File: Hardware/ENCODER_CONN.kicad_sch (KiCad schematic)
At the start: 22 parts, among them J11 PHB2.0-02-20PWZ, Q15 SI2305, Q17 SS8050, U31 MS2575T, U32 TXB0104RUTR, U33 MS2575T

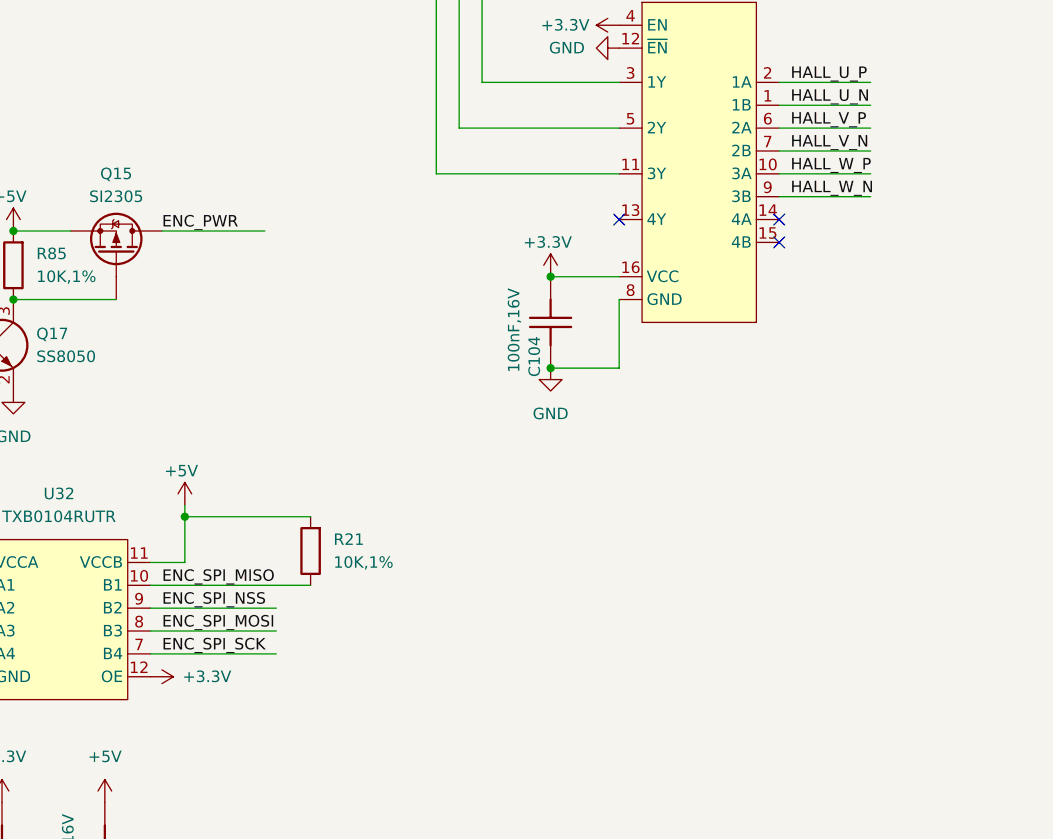
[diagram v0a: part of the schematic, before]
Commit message: 新增ESC IO引出，ESC CTR LED，EUI接口
编码器接口电源输出加保险，SPI加ESD
PY32ADC外部接口加ESD
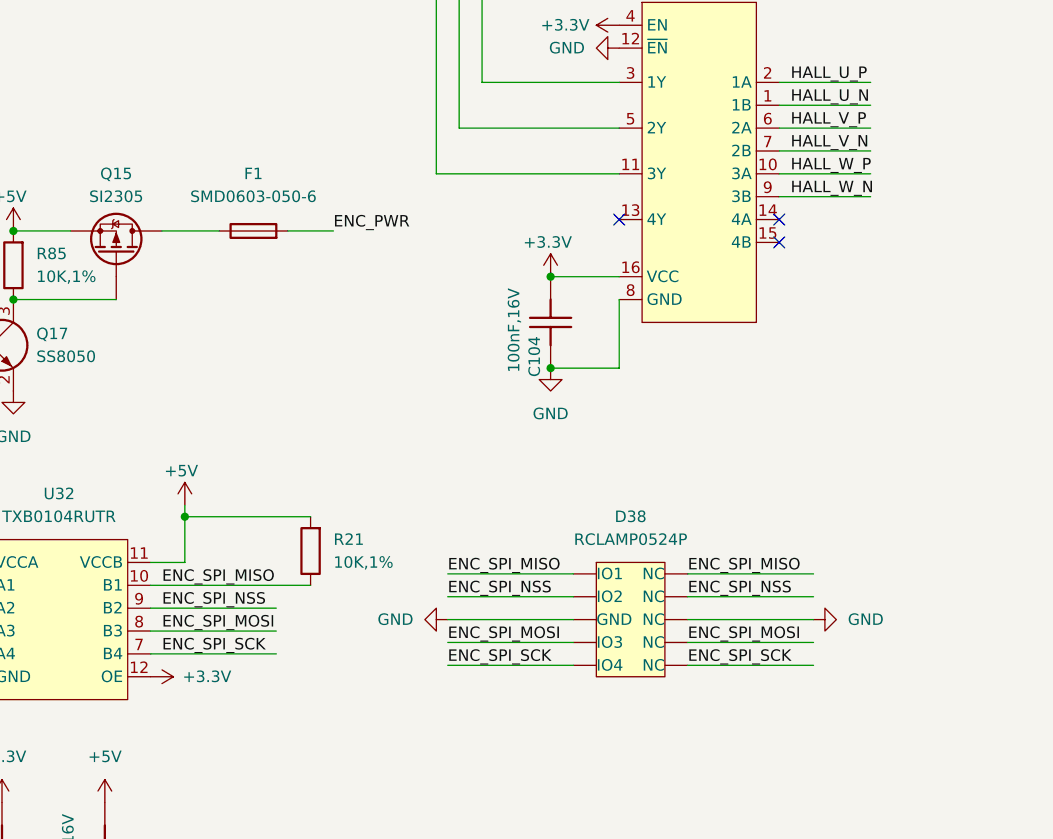
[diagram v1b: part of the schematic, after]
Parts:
- added D38: RCLAMP0524P, Package_DFN_QFN:Diodes_UDFN-10_1.0x2.5mm_P0.5mm, symbol HPM6280Foc:RCLAMP0524P
- added F1: SMD0603-050-6, Fuse:Fuse_0603_1608Metric, symbol HPM6280Foc:SMD0603-050-6
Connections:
- net ENC_PWR: now also F1.2; no longer Q15.3 (D)
- net ENC_SPI_MISO: now also D38.1 (IO1), D38.10 (NC)
- net ENC_SPI_MOSI: now also D38.4 (IO3), D38.7 (NC)
- net ENC_SPI_NSS: now also D38.2 (IO2), D38.9 (NC)
- net ENC_SPI_SCK: now also D38.5 (IO4), D38.6 (NC)
- net GND: now also D38.3 (GND), D38.8 (NC)
- new net: F1.1, Q15.3 (D)

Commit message: 拉线
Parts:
- renumbered C100 to C107, C103 to C110, C104 to C111, C105 to C112, C106 to C113, D38 to D39, F1 to F2, J11 to J12, NT21 to NT22, Q15 to Q16, Q17 to Q18, R21 to R22, R77 to R86, R78 to R87, R79 to R88, R80 to R89, R81 to R90, R82 to R91, R83 to R92, R84 to R93, R85 to R94, U31 to U35, U32 to U36, U33 to U37

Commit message: 修存档拉线
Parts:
- renumbered C107 to C79, C110 to C80, C111 to C81, C112 to C82, C113 to C83, J12 to J13, NT22 to NT21, Q16 to Q17, R86 to R79, R87 to R80, R88 to R81, R89 to R82, R90 to R83, R91 to R84, R92 to R85, R94 to R86, R93 to R87, R22 to R88, U35 to U39, U37 to U40, U36 to U41

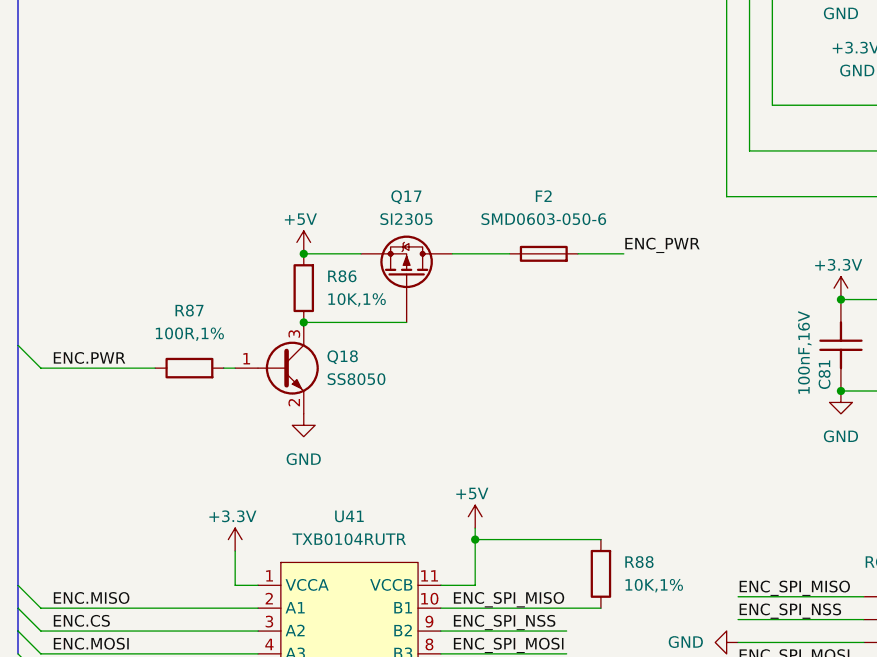
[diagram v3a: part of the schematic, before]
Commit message: 拉线，增加刹车电阻
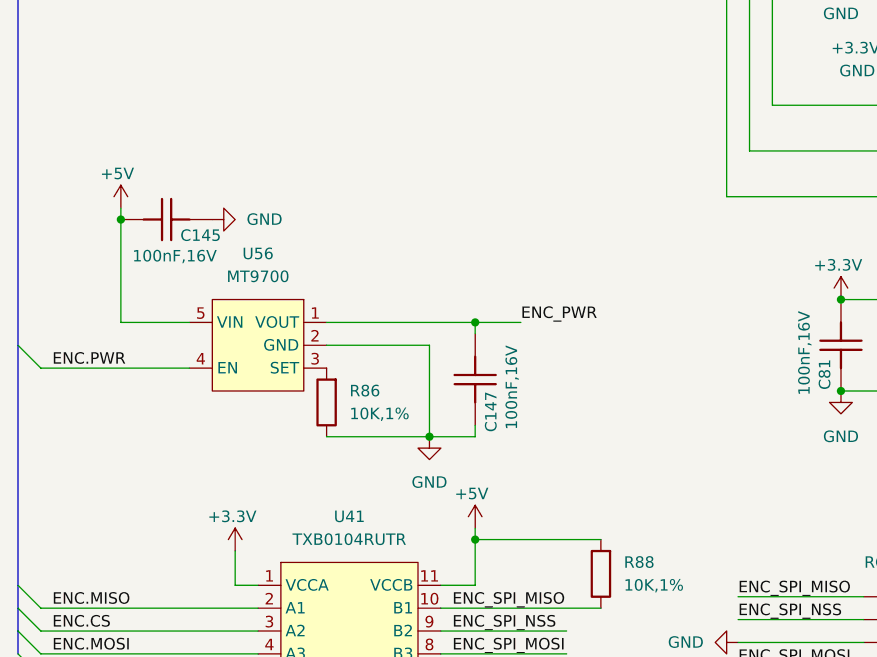
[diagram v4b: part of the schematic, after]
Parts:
- removed F2: SMD0603-050-6, Fuse:Fuse_0603_1608Metric, symbol HPM6280Foc:SMD0603-050-6
- removed Q17: SI2305, Package_TO_SOT_SMD:SOT-23-3, symbol HPM6280Foc:SI2305
- removed Q18: SS8050, Package_TO_SOT_SMD:SOT-23, symbol Transistor_BJT:SS8050
- removed R87: 100R,1%, Resistor_SMD:R_0402_1005Metric, symbol HPM6280Foc:0402WGF1000TCE
- added C145, C147: 100nF,16V, Capacitor_SMD:C_0402_1005Metric, symbol HPM6280Foc:CC0402KRX7R7BB104
- added U56: MT9700, Package_TO_SOT_SMD:SOT-23-5, symbol HPM6280Foc:MT9700
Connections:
- net +5V: now also C145.1, U56.5 (VIN); no longer R86.2
- net ENC.PWR: now also U56.4 (EN)
- net ENC_PWR: now also C147.2, U56.1 (VOUT)
- net GND: now also R86.1, C145.2, C147.1, U56.2 (GND)
- new net: R86.2, U56.3 (SET)

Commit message: PCB和foc_demo
PCB：
部分信号增加测试点
半桥增加栅极电容和RC吸收（待定），泄放mos是否需要栅极电容待测
软件：
增加foc_demo半成品
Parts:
- added TP1, TP10, TP12, TP14, TP16, TP18, TP3, TP4, TP6, TP8: ~, Library:test_point_0.5mm, symbol HPM6280Foc:test_point
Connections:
- net ENC.A: now also TP14.1
- net ENC.B: now also TP16.1
- net ENC.CLK: now also TP3.1
- net ENC.CS: now also TP4.1
- net ENC.MISO: now also TP6.1
- net ENC.MOSI: now also TP1.1
- net ENC.U: now also TP8.1
- net ENC.V: now also TP10.1
- net ENC.W: now also TP12.1
- net ENC.Z: now also TP18.1

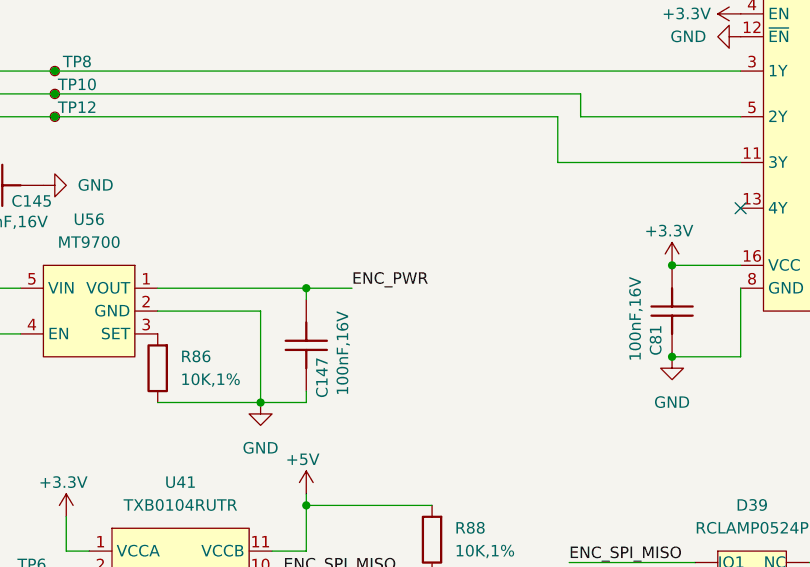
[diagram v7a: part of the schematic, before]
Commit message: PCB：风扇增加控制IO，泄放驱动增加使能引脚，485编码器电源接入控制
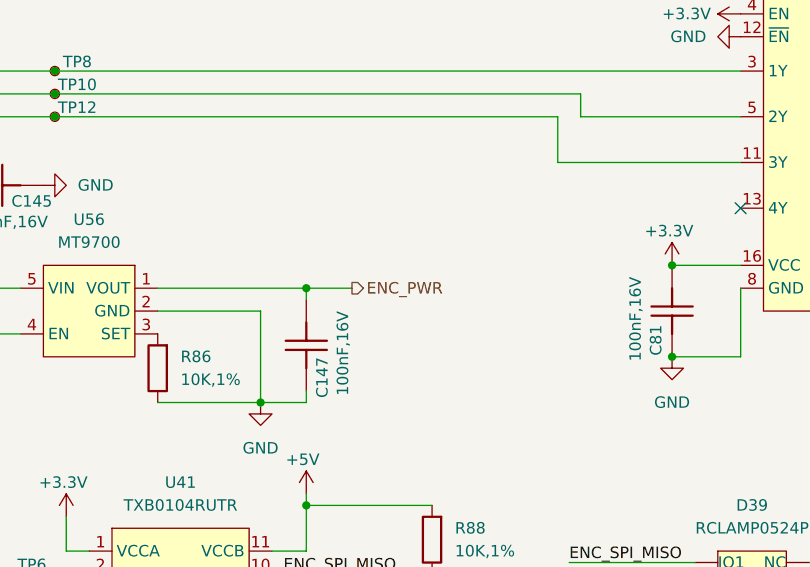
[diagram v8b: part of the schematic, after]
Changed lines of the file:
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@@
-		)
-	)
-	(label "ENC_PWR"
-		(at 85.09 107.95 0)
-		(effects
-			(font
-				(size 1.27 1.27)
-			)
-			(justify left bottom)
 		)
 	)
@@
 		)
 	)
+	(hierarchical_label "ENC_PWR"
+		(shape output)
+		(at 85.09 107.95 0)
+		(effects
+			(font
+				(size 1.27 1.27)
+			)
+			(justify left)
+		)
+	)
